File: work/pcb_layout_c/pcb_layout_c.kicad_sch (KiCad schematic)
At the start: 12 parts, among them IC1 TS02-66-50-BK-100-SCR-D, J1 Conn_01x15_Pin, U1 PIC24FJ64GA002-X_SP

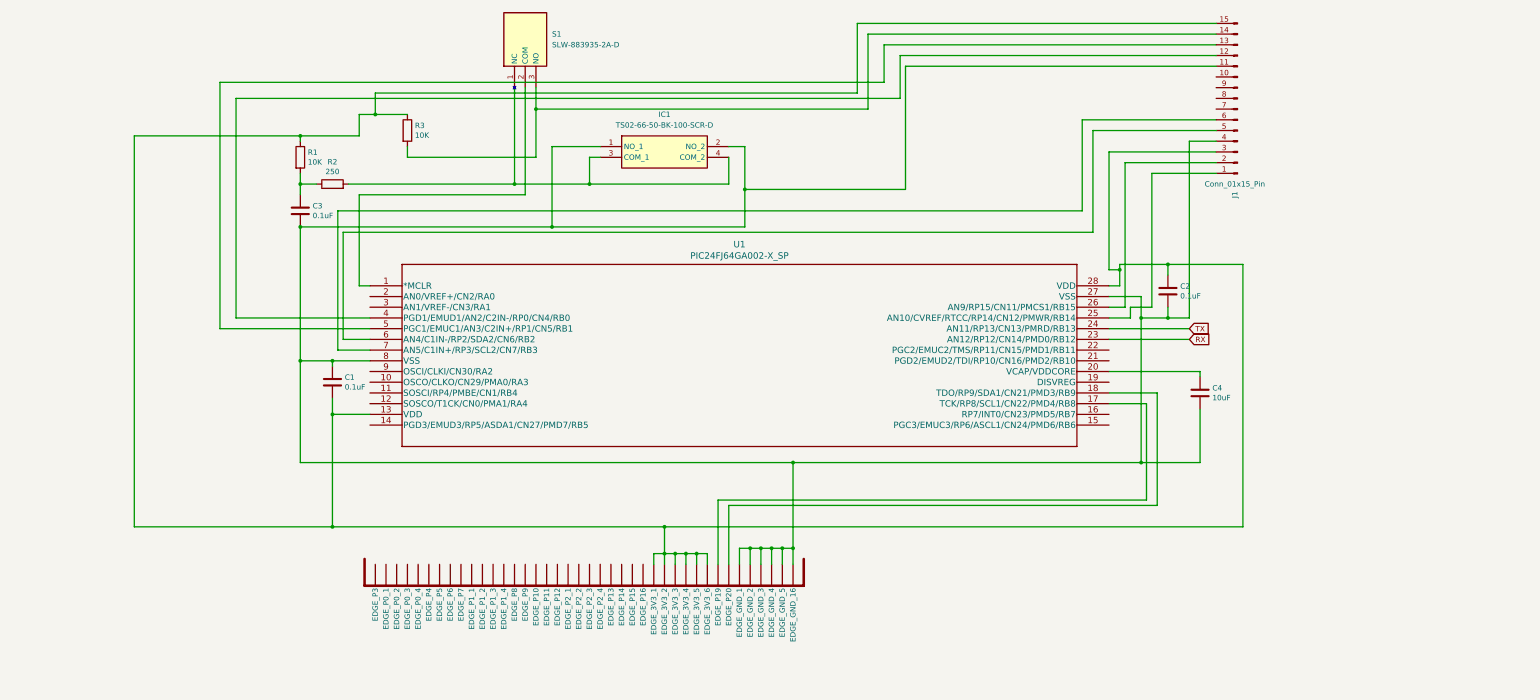
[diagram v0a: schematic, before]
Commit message: Issue #21 & Issue #23 Create KiCad schematic Update Symbol_Footprint directory
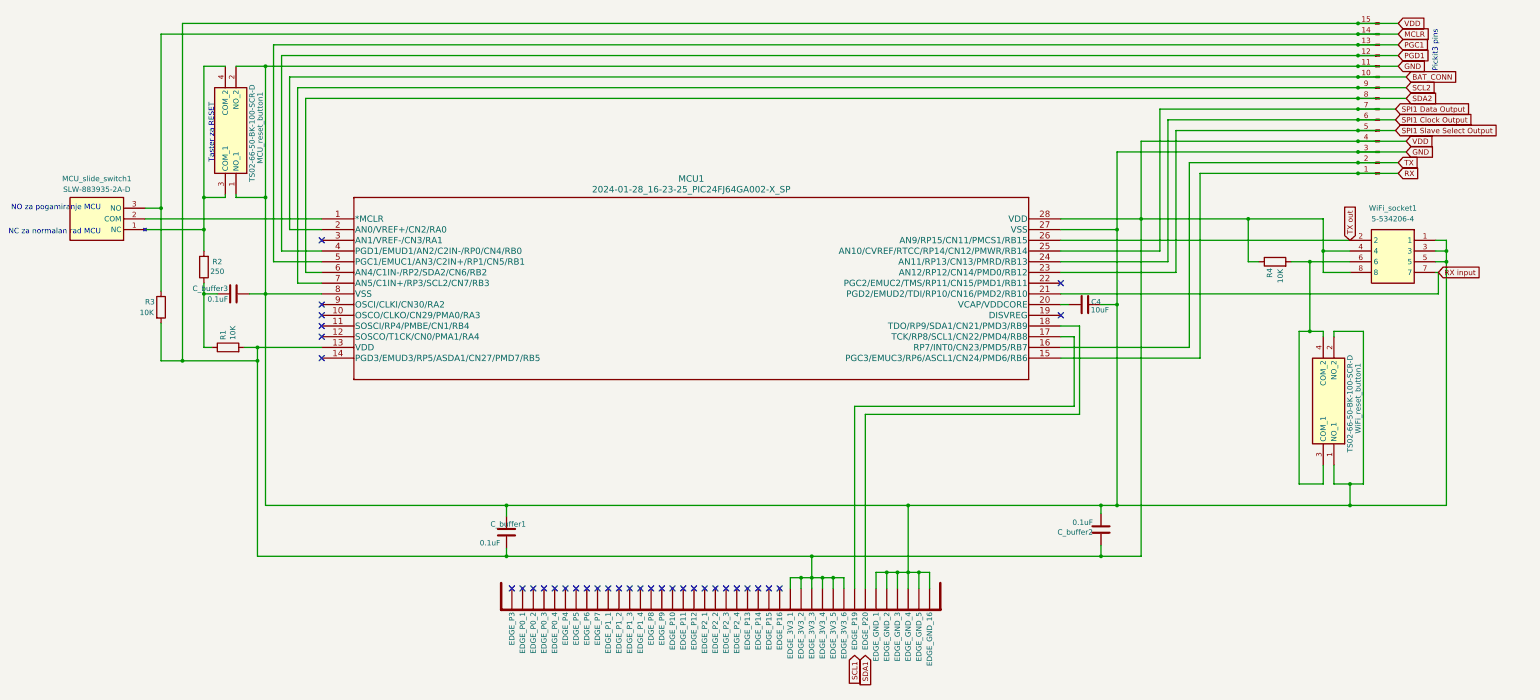
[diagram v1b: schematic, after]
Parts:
- removed C1, C2, C3: 0.1uF, symbol Device:C
- removed IC1: TS02-66-50-BK-100-SCR-D, TS026650BK100SCRD, symbol Button:TS02-66-50-BK-100-SCR-D
- removed S1: SLW-883935-2A-D, SLW8839352AD, symbol Slide Switch:SLW-883935-2A-D
- removed U1: PIC24FJ64GA002-X_SP, PIC24FJ64GA002:SPDIP28_300MC_MCH, symbol KiCad_Project-rescue:PIC24FJ64GA002-X_SP-2024-01-28_16-23-25
- added C_buffer1, C_buffer2, C_buffer3: 0.1uF, C01uF:CAPC1608X95N, symbol Device:C
- added MCU1: 2024-01-28_16-23-25_PIC24FJ64GA002-X_SP, mcu_socket_1-2199298-9:DIP762W60P254L3556H510Q28, symbol pcb_layout_c-rescue:PIC24FJ64GA002-X_SP-2024-01-28_16-23-25
- added MCU_reset_button1, WiFi_reset_button1: TS02-66-50-BK-100-SCR-D, TS02-66-50-BK-100-SCR-D:TS026650BK100SCRD, symbol Button:TS02-66-50-BK-100-SCR-D
- added MCU_slide_switch1: SLW-883935-2A-D, SLW-883935-2A-D:SLW8839352AD, symbol Slide Switch:SLW-883935-2A-D
- added R4: 10K, R10K:RESC3216X60N, symbol Device:R
- added WiFi_socket1: 5-534206-4, 2x4_pin_socket:RHDR8W69P254_2X4_1016X503X877P, symbol 2x4_Pin_Socket:5-534206-4
- C4: footprint (none) -> C10uF:CAPC3225X210N
- J1: footprint (none) -> Connector_PinHeader_2.54mm:PinHeader_1x15_P2.54mm_Vertical
- R1, R3: footprint (none) -> R10K:RESC3216X60N
- R2: footprint (none) -> R240:RESC3216X70N
- edge_connector1: renamed from 1; value ~ -> edge_connector1; footprint untitled:BBC_EDGE -> Edge_connector:BBC_EDGE
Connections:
- net RX: now also J1.1 (Pin_1), MCU1.15 (PGC3/EMUC3/RP6/ASCL1/CN24/PMD6/RB6)
- net TX: now also J1.2 (Pin_2), MCU1.16 (RP7/INT0/CN23/PMD5/RB7)
- net VDD: now reaches J1.15 (Pin_15), edge_connector1.P$27 (EDGE_3V3_1), edge_connector1.P$28 (EDGE_3V3_2), edge_connector1.P$29 (EDGE_3V3_3), edge_connector1.P$30 (EDGE_3V3_4), edge_connector1.P$31 (EDGE_3V3_5), edge_connector1.P$32 (EDGE_3V3_6), edge_connector1.P$67 (EDGE_3V3_1), edge_connector1.P$68 (EDGE_3V3_2), edge_connector1.P$69 (EDGE_3V3_3), edge_connector1.P$70 (EDGE_3V3_4), edge_connector1.P$71 (EDGE_3V3_5), edge_connector1.P$72 (EDGE_3V3_6)
- net VDD: now also J1.4 (Pin_4), R1.2, R3.2, C_buffer1.2, C_buffer2.1, MCU1.13 (VDD), MCU1.28 (VDD), R4.1, WiFi_socket1.4, WiFi_socket1.8; no longer J1.3 (Pin_3), R1.1, R3.1
- net at edge_connector1.P$33 (EDGE_P19), edge_connector1.P$73 (EDGE_P19): now also MCU1.17 (TCK/RP8/SCL1/CN22/PMD4/RB8)
- net at edge_connector1.P$34 (EDGE_P20), edge_connector1.P$74 (EDGE_P20): now also MCU1.18 (TDO/RP9/SDA1/CN21/PMD3/RB9)
- net at C4.1: now also MCU1.20 (VCAP/VDDCORE)
- net GND: now reaches C4.2, J1.11 (Pin_11), edge_connector1.P$35 (EDGE_GND_1), edge_connector1.P$36 (EDGE_GND_2), edge_connector1.P$37 (EDGE_GND_3), edge_connector1.P$38 (EDGE_GND_4), edge_connector1.P$39 (EDGE_GND_5), edge_connector1.P$40 (EDGE_GND_16), edge_connector1.P$75 (EDGE_GND_1), edge_connector1.P$76 (EDGE_GND_2), edge_connector1.P$77 (EDGE_GND_3), edge_connector1.P$78 (EDGE_GND_4), edge_connector1.P$79 (EDGE_GND_5), edge_connector1.P$80 (EDGE_GND_16)
- net GND: now also J1.3 (Pin_3), C_buffer1.1, C_buffer2.2, C_buffer3.2, MCU1.27 (VSS), MCU1.8 (VSS), MCU_reset_button1.1 (NO_1), MCU_reset_button1.2 (NO_2), WiFi_reset_button1.1 (NO_1), WiFi_reset_button1.2 (NO_2), WiFi_socket1.1, WiFi_socket1.3, WiFi_socket1.5; no longer J1.4 (Pin_4)
- net PGD1: now reaches J1.12 (Pin_12)
- net PGD1: now also MCU1.4 (PGD1/EMUD1/AN2/C2IN-/RP0/CN4/RB0)
- net PGC1: now reaches J1.13 (Pin_13)
- net PGC1: now also MCU1.5 (PGC1/EMUC1/AN3/C2IN+/RP1/CN5/RB1)
- net SPI1 Slave Select Output: now reaches J1.5 (Pin_5)
- net SPI1 Slave Select Output: now also MCU1.23 (AN12/RP12/CN14/PMD0/RB12)
- net SPI1 Clock Output: now reaches J1.6 (Pin_6)
- net SPI1 Clock Output: now also MCU1.24 (AN11/RP13/CN13/PMRD/RB13)
- net at R2.1: now also R1.1, C_buffer3.1; no longer R1.2
- net at R2.2: now also MCU_reset_button1.3 (COM_1), MCU_reset_button1.4 (COM_2), MCU_slide_switch1.1 (NC)
- net BAT_CONN: now reaches J1.10 (Pin_10)
- net BAT_CONN: now also MCU1.2 (AN0/VREF+/CN2/RA0)
- net MCLR: now reaches J1.14 (Pin_14)
- net MCLR: now also R3.1, MCU_slide_switch1.3 (NO); no longer R3.2
- net SPI1 Data Output: now reaches J1.7 (Pin_7)
- net SPI1 Data Output: now also MCU1.25 (AN10/CVREF/RTCC/RP14/CN12/PMWR/RB14)
- net SDA2: now reaches J1.8 (Pin_8)
- net SDA2: now also MCU1.6 (AN4/C1IN-/RP2/SDA2/CN6/RB2)
- net SCL2: now reaches J1.9 (Pin_9)
- net SCL2: now also MCU1.7 (AN5/C1IN+/RP3/SCL2/CN7/RB3)
- new net: MCU1.1 (*MCLR), MCU_slide_switch1.2 (COM)
- new net: R4.2, WiFi_reset_button1.3 (COM_1), WiFi_reset_button1.4 (COM_2), WiFi_socket1.6
- new net RX input: MCU1.21 (PGD2/EMUD2/TDI/RP10/CN16/PMD2/RB10), WiFi_socket1.7
- new net TX out: MCU1.26 (AN9/RP15/CN11/PMCS1/RB15), WiFi_socket1.2
- no-connect marks 0 -> 34
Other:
- note added: "NC za normalan rad MCU"
- note added: "NO za pogamiranje MCU"
- note added: "Pickit3 pins"
- note added: "Taster za RESET"

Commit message: Issue #22 : Kreiranje PCB dizajna cjelokupnog sistema
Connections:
- net GND: now also WiFi_socket1.7; no longer WiFi_socket1.1
- net RX input: now also WiFi_socket1.1; no longer WiFi_socket1.7
- net TX out: now also WiFi_socket1.8; no longer WiFi_socket1.2
- net VDD: now also WiFi_socket1.2, WiFi_socket1.6; no longer WiFi_socket1.4, WiFi_socket1.8
- net at R4.2, WiFi_reset_button1.3 (COM_1), WiFi_reset_button1.4 (COM_2): now also WiFi_socket1.4; no longer WiFi_socket1.6
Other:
- moved on the sheet: WiFi_socket1
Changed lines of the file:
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@@
-    (stroke (width 0) (type default))
-  )
-  (wire (pts (xy 325.12 67.945) (xy 322.58 67.945))
     (stroke (width 0) (type default))
   )
@@
     (stroke (width 0) (type default))
   )
+  (wire (pts (xy 233.68 67.945) (xy 302.26 67.945))
+    (stroke (width 0) (type default))
+  )
   (wire (pts (xy 30.48 78.105) (xy 30.48 80.645))
     (stroke (width 0) (type default))
@@
     (stroke (width 0) (type default))
   )
-  (wire (pts (xy 233.68 67.945) (xy 302.26 67.945))
-    (stroke (width 0) (type default))
-  )
   (wire (pts (xy 257.175 70.485) (xy 257.175 36.83))
     (stroke (width 0) (type default))
@@
   )
   (wire (pts (xy 46.99 21.59) (xy 304.165 21.59))
+    (stroke (width 0) (type default))
+  )
+  (wire (pts (xy 322.58 67.945) (xy 325.12 67.945))
     (stroke (width 0) (type default))
   )
@@
     )
   )
-  (global_label "TX out" (shape input) (at 302.26 67.945 90) (fields_autoplaced)
-    (effects (font (size 1.27 1.27)) (justify left))
-    (property "Intersheetrefs" "${INTERSHEET_REFS}" (at 302.26 59.4456 90)
+  (global_label "TX out" (shape input) (at 300.355 67.945 90) (fields_autoplaced)
+    (effects (font (size 1.27 1.27)) (justify left))
+    (property "Intersheetrefs" "${INTERSHEET_REFS}" (at 300.355 59.4456 90)
       (effects (font (size 1.27 1.27)) (justify left) hide)
     )
@@
     )
   )
-  (symbol (lib_id "2x4_Pin_Socket:5-534206-4") (at 322.58 67.945 0) (mirror y) (unit 1)
+  (symbol (lib_id "2x4_Pin_Socket:5-534206-4") (at 322.58 75.565 180) (unit 1)
     (in_bom yes) (on_board yes) (dnp no)
-    (property "Reference" "WiFi_socket1" (at 312.42 60.325 0)
+    (property "Reference" "WiFi_socket1" (at 312.42 83.185 0)
       (effects (font (size 1.27 1.27)))
     )
-    (property "Value" "5-534206-4" (at 312.42 62.865 0)
+    (property "Value" "5-534206-4" (at 312.42 80.645 0)
       (effects (font (size 1.27 1.27)))
     )
-    (property "Footprint" "2x4_pin_socket:RHDR8W69P254_2X4_1016X503X877P" (at 306.07 162.865 0)
-      (effects (font (size 1.27 1.27)) (justify left top) hide)
-    )
-    (property "Datasheet" "https://www.arrow.com/en/products/5-534206-4/te-connectivity" (at 306.07 262.865 0)
-      (effects (font (size 1.27 1.27)) (justify left top) hide)
-    )
-    (property "Height" "8.77" (at 306.07 462.865 0)
-      (effects (font (size 1.27 1.27)) (justify left top) hide)
-    )
-    (property "Mouser Part Number" "571-5-534206-4" (at 306.07 562.865 0)
-      (effects (font (size 1.27 1.27)) (justify left top) hide)
-    )
-    (property "Mouser Price/Stock" "https://www.mouser.co.uk/ProductDetail/TE-Connectivity/5-534206-4?qs=Eln3I3szM1ldJZZch%252BwNBQ%3D%3D" (at 306.07 662.865 0)
-      (effects (font (size 1.27 1.27)) (justify left top) hide)
-    )
-    (property "Manufacturer_Name" "TE Connectivity" (at 306.07 762.865 0)
-      (effects (font (size 1.27 1.27)) (justify left top) hide)
-    )
-    (property "Manufacturer_Part_Number" "5-534206-4" (at 306.07 862.865 0)
-      (effects (font (size 1.27 1.27)) (justify left top) hide)
-    )
+    (property "Footprint" "2x4_pin_socket:RHDR8W69P254_2X4_1016X503X877P" (at 306.07 -19.355 0)
+      (effects (font (size 1.27 1.27)) (justify left top) hide)
+    )
+    (property "Datasheet" "https://www.arrow.com/en/products/5-534206-4/te-connectivity" (at 306.07 -119.355 0)
+      (effects (font (size 1.27 1.27)) (justify left top) hide)
+    )
+    (property "Height" "8.77" (at 306.07 -319.355 0)
+      (effects (font (size 1.27 1.27)) (justify left top) hide)
+    )
+    (property "Mouser Part Number" "571-5-534206-4" (at 306.07 -419.355 0)
+      (effects (font (size 1.27 1.27)) (justify left top) hide)
+    )
+    (property "Mouser Price/Stock" "https://www.mouser.co.uk/ProductDetail/TE-Connectivity/5-534206-4?qs=Eln3I3szM1ldJZZch%252BwNBQ%3D%3D" (at 306.07 -519.355 0)
+      (effects (font (size 1.27 1.27)) (justify left top) hide)
+    )
+    (property "Manufacturer_Name" "TE Connectivity" (at 306.07 -619.355 0)
+      (effects (font (size 1.27 1.27)) (justify left top) hide)
+    )
+    (property "Manufacturer_Part_Number" "5-534206-4" (at 306.07 -719.355 0)
+      (effects (font (size 1.27 1.27)) (justify left top) hide)
+    )

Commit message: Issue #27 : Promjena velicine sheeta na KiCad schemi Promijenjana velicina okvira na .kicad_sch fajlu
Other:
- moved on the sheet: C4, C_buffer1, C_buffer2, C_buffer3, MCU1, MCU_reset_button1, MCU_slide_switch1, R1, R2, R3, R4, WiFi_reset_button1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
